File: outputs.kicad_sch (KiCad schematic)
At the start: 56 parts, among them Q2 DTC113Z, Q3 DTC113Z, Q4 DTC113Z, Q5 DTC113Z, Q6 DTC113Z, Q7 DTC113Z, Q8 DTC113Z, Q9 DTC113Z, U10 AQH0213, U11 AQH0213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

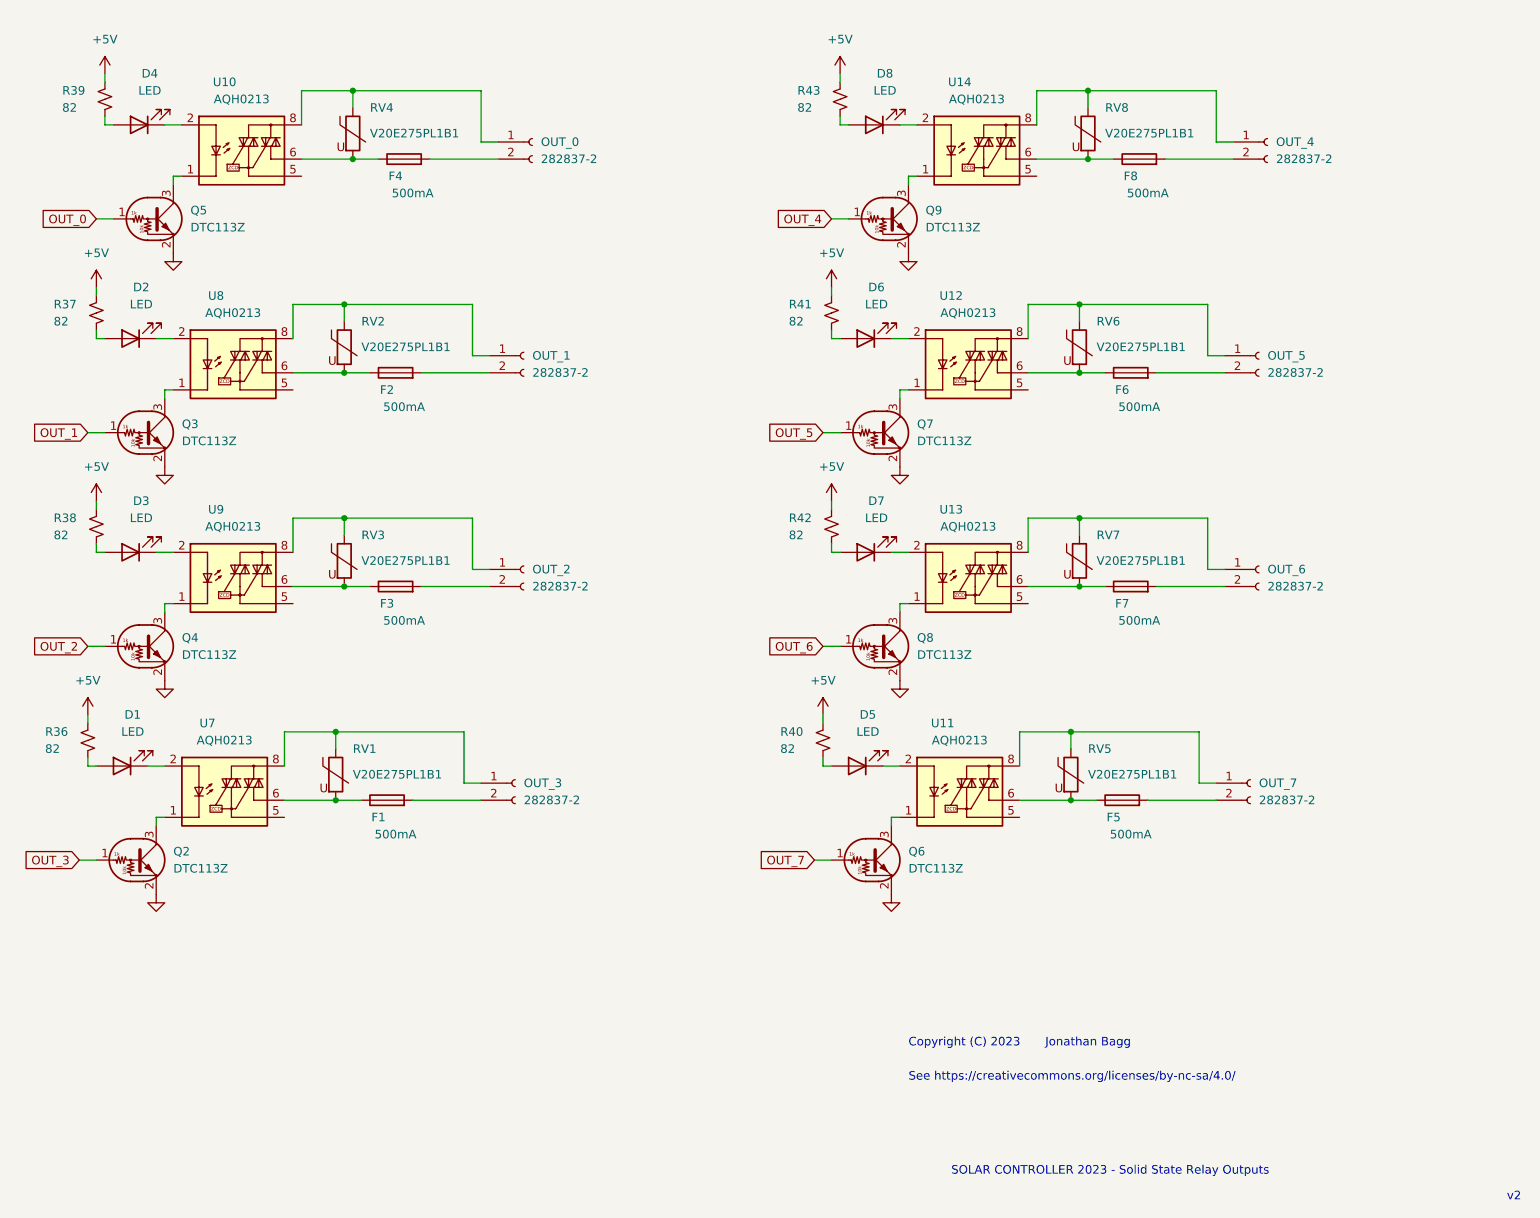
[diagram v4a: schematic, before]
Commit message: replace sensor wire esd caps with TVSs
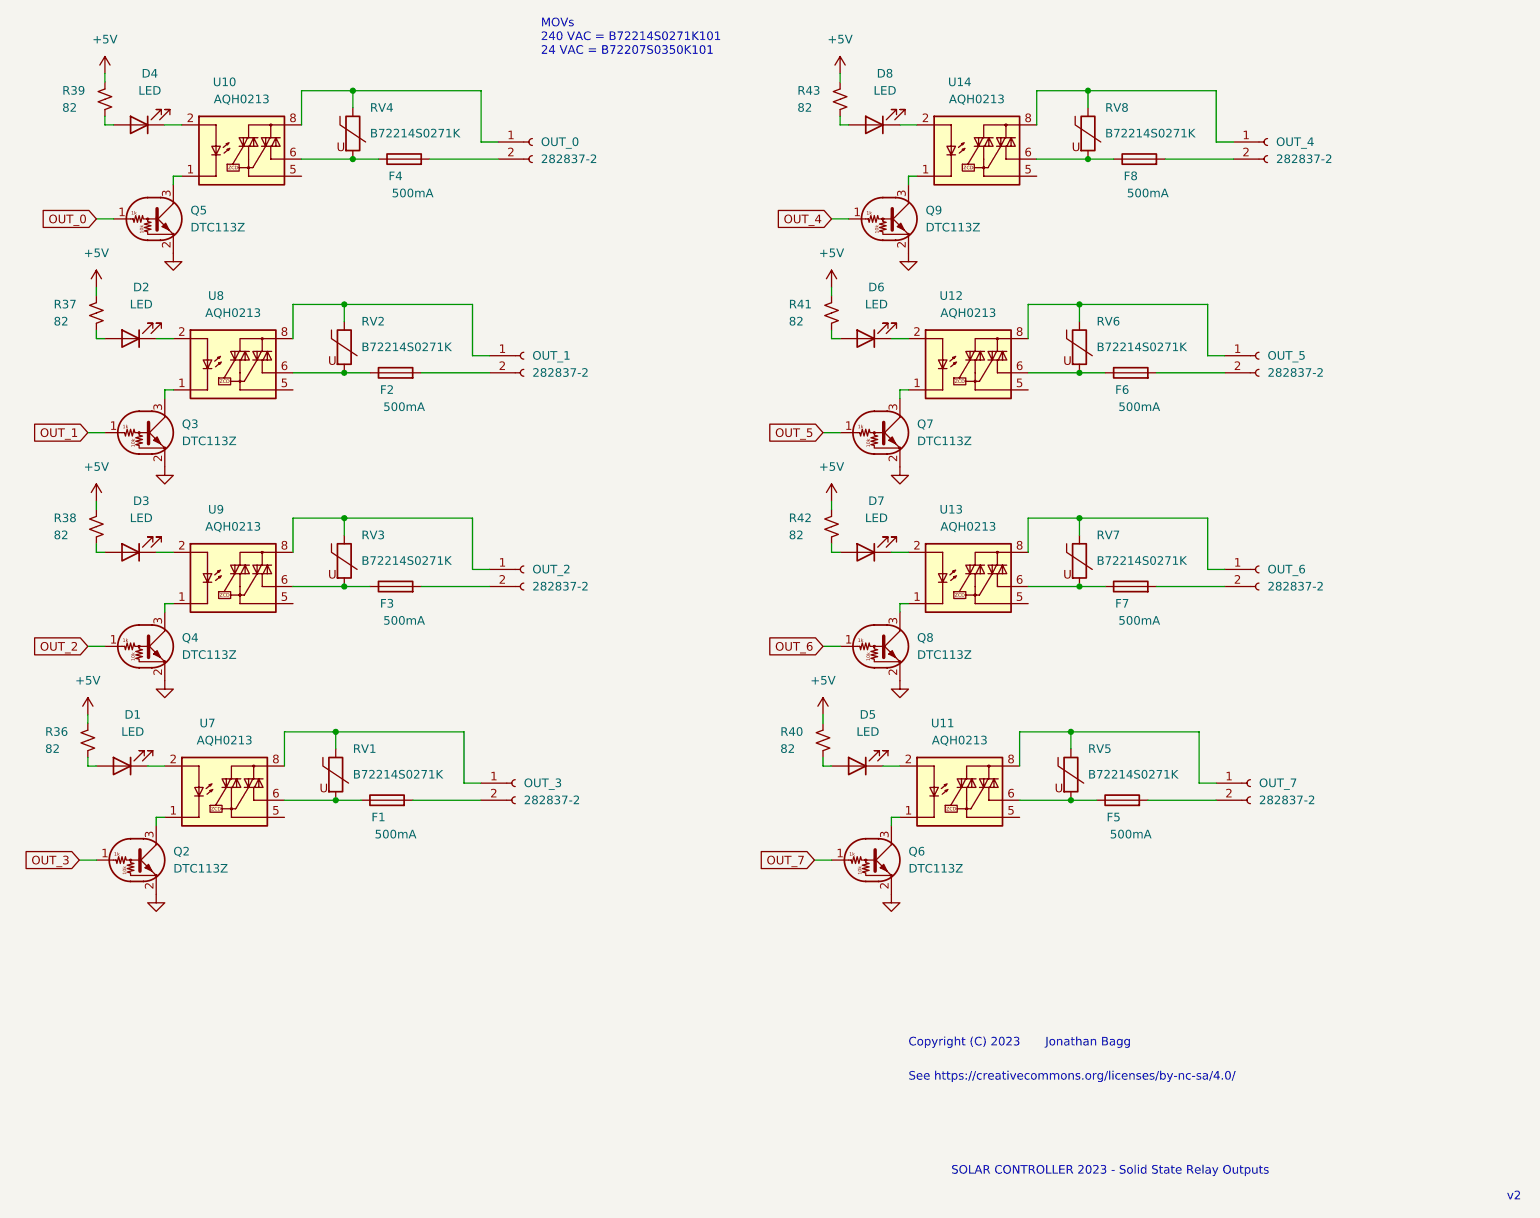
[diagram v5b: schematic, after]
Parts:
- RV1, RV2, RV3, RV4, RV5, RV6, RV7, RV8: value V20E275PL1B1 -> B72214S0271K; Digikey (none) -> 495-1412-ND
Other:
- note added: "MOVs 240 VAC = B72214S0271K101 24 VAC = B72207S0350K101"
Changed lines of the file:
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@@
+    (effects (font (size 1.27 1.27)) (justify left bottom))
+  )
+  (text "MOVs\n240 VAC = B72214S0271K101\n24 VAC = B72207S0350K101"
+    (at 128.27 24.13 0)
     (effects (font (size 1.27 1.27)) (justify left bottom))
   )
@@
       (effects (font (size 1.27 1.27)) (justify left))
     )
-    (property "Value" "V20E275PL1B1" (id 1) (at 101.6 67.31 0)
+    (property "Value" "B72214S0271K" (id 1) (at 101.6 67.31 0)
       (effects (font (size 1.27 1.27)) (justify left))
     )
@@
     )
     (property "Datasheet" "~" (id 3) (at 99.06 67.31 0)
+      (effects (font (size 1.27 1.27)) hide)
+    )
+    (property "Digikey" "495-1412-ND" (id 4) (at 99.06 67.31 0)
       (effects (font (size 1.27 1.27)) hide)
     )
@@
       (effects (font (size 1.27 1.27)) (justify left))
     )
-    (property "Value" "V20E275PL1B1" (id 1) (at 101.6 99.06 0)
+    (property "Value" "B72214S0271K" (id 1) (at 101.6 99.06 0)
       (effects (font (size 1.27 1.27)) (justify left))
     )
@@
       (effects (font (size 1.27 1.27)) hide)
     )
+    (property "Digikey" "495-1412-ND" (id 4) (at 99.06 99.06 0)
+      (effects (font (size 1.27 1.27)) hide)
+    )
     (pin "1")
     (pin "2")
@@
       (effects (font (size 1.27 1.27)) (justify left))
     )
-    (property "Value" "V20E275PL1B1" (id 1) (at 212.09 35.56 0)
+    (property "Value" "B72214S0271K" (id 1) (at 212.09 35.56 0)
       (effects (font (size 1.27 1.27)) (justify left))
     )
@@
     )
     (property "Datasheet" "~" (id 3) (at 209.55 35.56 0)
+      (effects (font (size 1.27 1.27)) hide)
+    )
+    (property "Digikey" "495-1412-ND" (id 4) (at 209.55 35.56 0)
       (effects (font (size 1.27 1.27)) hide)
     )
@@
       (effects (font (size 1.27 1.27)) (justify left))
     )
-    (property "Value" "V20E275PL1B1" (id 1) (at 210.82 99.06 0)
+    (property "Value" "B72214S0271K" (id 1) (at 210.82 99.06 0)
       (effects (font (size 1.27 1.27)) (justify left))
     )
@@
     )
     (property "Datasheet" "~" (id 3) (at 208.28 99.06 0)
+      (effects (font (size 1.27 1.27)) hide)
+    )
+    (property "Digikey" "495-1412-ND" (id 4) (at 208.28 99.06 0)
       (effects (font (size 1.27 1.27)) hide)
     )
@@
       (effects (font (size 1.27 1.27)) (justify left))
     )
-    (property "Value" "V20E275PL1B1" (id 1) (at 209.55 130.81 0)
+    (property "Value" "B72214S0271K" (id 1) (at 209.55 130.81 0)
       (effects (font (size 1.27 1.27)) (justify left))
     )
@@
       (effects (font (size 1.27 1.27)) hide)
     )
+    (property "Digikey" "495-1412-ND" (id 4) (at 207.01 130.81 0)
+      (effects (font (size 1.27 1.27)) hide)
+    )
     (pin "1")
     (pin "2")
@@
       (effects (font (size 1.27 1.27)) (justify left))
     )
-    (property "Value" "V20E275PL1B1" (id 1) (at 102.87 35.56 0)
+    (property "Value" "B72214S0271K" (id 1) (at 102.87 35.56 0)
       (effects (font (size 1.27 1.27)) (justify left))
     )
@@
     )
     (property "Datasheet" "~" (id 3) (at 100.33 35.56 0)
+      (effects (font (size 1.27 1.27)) hide)
+    )
+    (property "Digikey" "495-1412-ND" (id 4) (at 100.33 35.56 0)
       (effects (font (size 1.27 1.27)) hide)
     )
@@
       (effects (font (size 1.27 1.27)) (justify left))
     )
-    (property "Value" "V20E275PL1B1" (id 1) (at 210.82 67.31 0)
+    (property "Value" "B72214S0271K" (id 1) (at 210.82 67.31 0)
       (effects (font (size 1.27 1.27)) (justify left))
     )
@@
       (effects (font (size 1.27 1.27)) hide)
     )
+    (property "Digikey" "495-1412-ND" (id 4) (at 208.28 67.31 0)
+      (effects (font (size 1.27 1.27)) hide)
+    )
     (pin "1")
     (pin "2")
@@
       (effects (font (size 1.27 1.27)) (justify left))
     )
-    (property "Value" "V20E275PL1B1" (id 1) (at 100.33 130.81 0)
+    (property "Value" "B72214S0271K" (id 1) (at 100.33 130.81 0)
       (effects (font (size 1.27 1.27)) (justify left))
     )
@@
       (effects (font (size 1.27 1.27)) hide)
     )
+    (property "Digikey" "495-1412-ND" (id 4) (at 97.79 130.81 0)
+      (effects (font (size 1.27 1.27)) hide)
+    )

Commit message: generate gerbers
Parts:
- RV1, RV2, RV3, RV4, RV5, RV6, RV7, RV8: footprint Varistor:RV_Disc_D9mm_W3.3mm_P5mm -> Capacitor_THT:C_Rect_L9.0mm_W2.5mm_P7.50mm_MKT
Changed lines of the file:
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@@
       (effects (font (size 1.27 1.27)) (justify left))
     )
-    (property "Footprint" "Varistor:RV_Disc_D9mm_W3.3mm_P5mm" (id 2) (at 97.282 67.31 90)
+    (property "Footprint" "Capacitor_THT:C_Rect_L9.0mm_W2.5mm_P7.50mm_MKT" (id 2) (at 97.282 67.31 90)
       (effects (font (size 1.27 1.27)) hide)
     )
@@
       (effects (font (size 1.27 1.27)) (justify left))
     )
-    (property "Footprint" "Varistor:RV_Disc_D9mm_W3.3mm_P5mm" (id 2) (at 97.282 99.06 90)
+    (property "Footprint" "Capacitor_THT:C_Rect_L9.0mm_W2.5mm_P7.50mm_MKT" (id 2) (at 97.282 99.06 90)
       (effects (font (size 1.27 1.27)) hide)
     )
@@
       (effects (font (size 1.27 1.27)) (justify left))
     )
-    (property "Footprint" "Varistor:RV_Disc_D9mm_W3.3mm_P5mm" (id 2) (at 207.772 35.56 90)
+    (property "Footprint" "Capacitor_THT:C_Rect_L9.0mm_W2.5mm_P7.50mm_MKT" (id 2) (at 207.772 35.56 90)
       (effects (font (size 1.27 1.27)) hide)
     )
@@
       (effects (font (size 1.27 1.27)) (justify left))
     )
-    (property "Footprint" "Varistor:RV_Disc_D9mm_W3.3mm_P5mm" (id 2) (at 206.502 99.06 90)
+    (property "Footprint" "Capacitor_THT:C_Rect_L9.0mm_W2.5mm_P7.50mm_MKT" (id 2) (at 206.502 99.06 90)
       (effects (font (size 1.27 1.27)) hide)
     )
@@
       (effects (font (size 1.27 1.27)) (justify left))
     )
-    (property "Footprint" "Varistor:RV_Disc_D9mm_W3.3mm_P5mm" (id 2) (at 205.232 130.81 90)
+    (property "Footprint" "Capacitor_THT:C_Rect_L9.0mm_W2.5mm_P7.50mm_MKT" (id 2) (at 205.232 130.81 90)
       (effects (font (size 1.27 1.27)) hide)
     )
@@
       (effects (font (size 1.27 1.27)) (justify left))
     )
-    (property "Footprint" "Varistor:RV_Disc_D9mm_W3.3mm_P5mm" (id 2) (at 98.552 35.56 90)
+    (property "Footprint" "Capacitor_THT:C_Rect_L9.0mm_W2.5mm_P7.50mm_MKT" (id 2) (at 98.552 35.56 90)
       (effects (font (size 1.27 1.27)) hide)
     )
@@
       (effects (font (size 1.27 1.27)) (justify left))
     )
-    (property "Footprint" "Varistor:RV_Disc_D9mm_W3.3mm_P5mm" (id 2) (at 206.502 67.31 90)
+    (property "Footprint" "Capacitor_THT:C_Rect_L9.0mm_W2.5mm_P7.50mm_MKT" (id 2) (at 206.502 67.31 90)
       (effects (font (size 1.27 1.27)) hide)
     )
@@
       (effects (font (size 1.27 1.27)) (justify left))
     )
-    (property "Footprint" "Varistor:RV_Disc_D9mm_W3.3mm_P5mm" (id 2) (at 96.012 130.81 90)
-      (effects (font (size 1.27 1.27)) hide)
-    )
+    (property "Footprint" "Capacitor_THT:C_Rect_L9.0mm_W2.5mm_P7.50mm_MKT" (id 2) (at 96.012 130.81 90)
+      (effects (font (size 1.27 1.27)) hide)
+    )

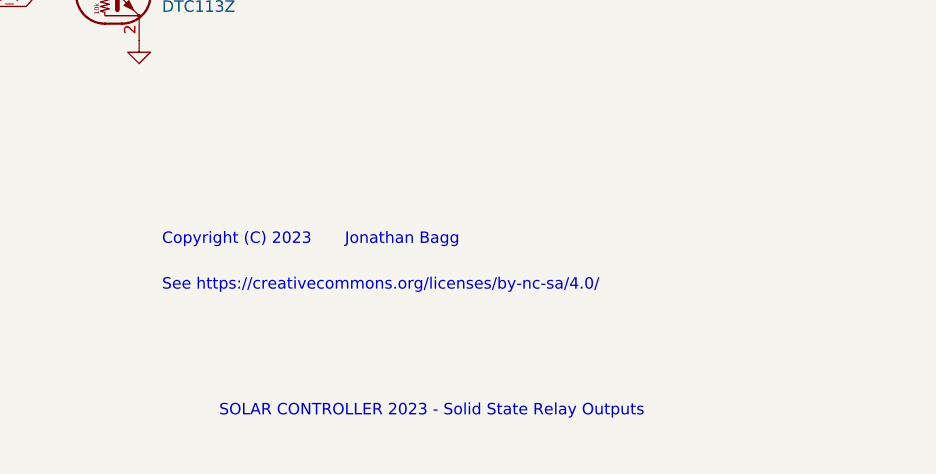
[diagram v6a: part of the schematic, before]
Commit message: add github link to title block and print schematic pdf
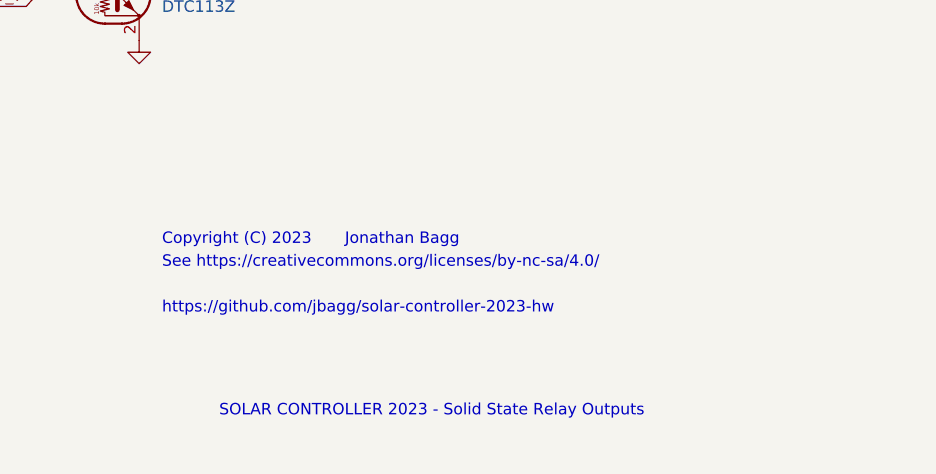
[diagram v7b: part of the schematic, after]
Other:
- note added: "https://github.com/jbagg/solar-controller-2023-hw"
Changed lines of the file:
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@@
   )
   (text "See https://creativecommons.org/licenses/by-nc-sa/4.0/"
-    (at 182.88 176.53 0)
+    (at 182.88 173.99 0)
     (effects (font (size 1.27 1.27)) (justify left bottom))
   )
+  (text "https://github.com/jbagg/solar-controller-2023-hw" (at 182.88 179.07 0)
+    (effects (font (size 1.27 1.27)) (justify left bottom))
+  )
